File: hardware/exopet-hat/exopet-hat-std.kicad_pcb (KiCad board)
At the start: 2 copper layers, 65 x 56 mm, 77 parts, among them J1 BarrelJack_CUI_PJ-102AH_Horiz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, J10 TerminalBlock_Phoenix_PT-1,5-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, J11 TerminalBlock_Phoenix_PT-1,5-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, J13 TerminalBlock_Phoenix_PT-1,5-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, J14 TerminalBlock_Phoenix_PT-1,5-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, J3 PinSocket_2x20_P2.54mm_Vertic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, J4 TerminalBlock_Phoenix_PT-1,5-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, J8 TerminalBlock_Phoenix_PT-1,5-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, J9 TerminalBlock_Phoenix_PT-1,5-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, K1 Relay_SPDT_Omron-G5LE-1, K2 Relay_SPDT_Omron-G5LE-1, K3 Relay_SPDT_Omron-G5LE-1, K4 Relay_SPDT_Omron-G5LE-1, Q1 TO-252-2, U2 SOIC-16_3.9x9.9mm_P1.27mm, U4 SOIC-8_3.9x4.9mm_P1.27mm, U5 D_SOD-323, U6 SOT-23-6, U7 MSOP-10_3x3mm_P0.5mm

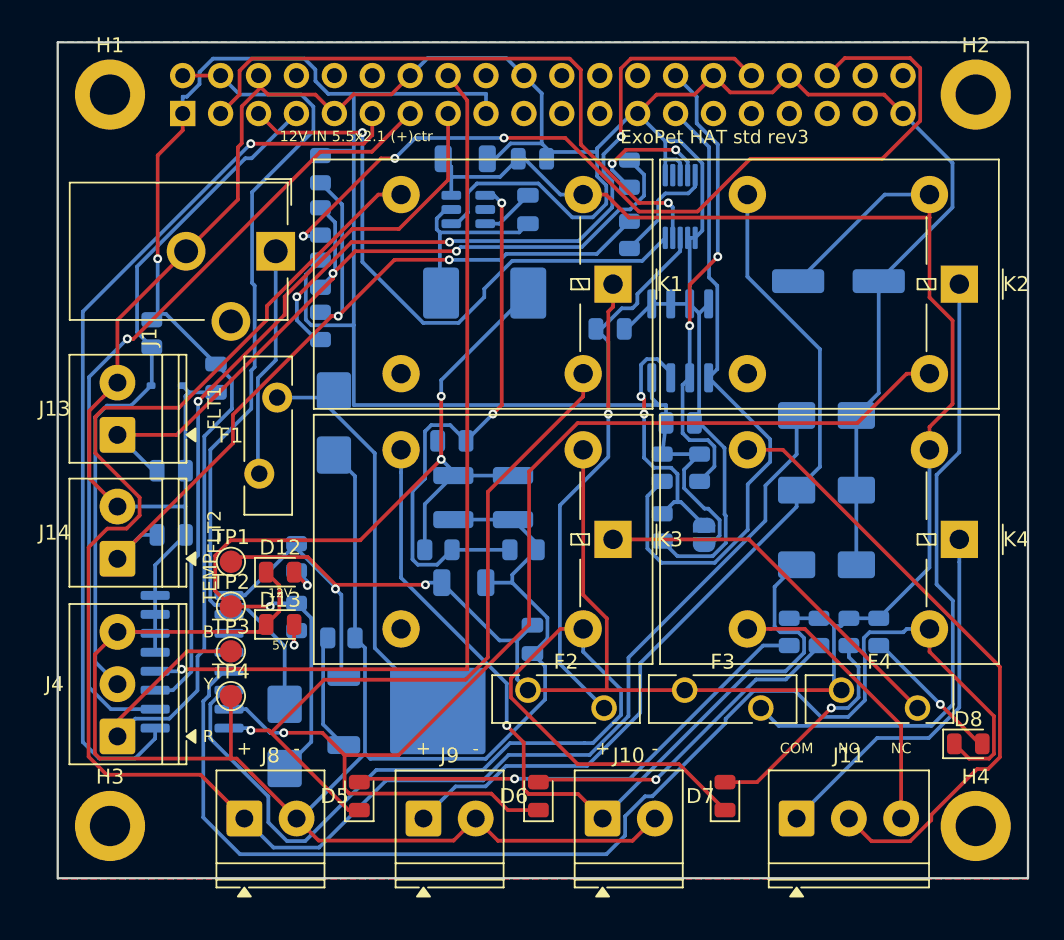
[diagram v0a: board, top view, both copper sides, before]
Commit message: HAT std: verified JLC part numbers + DFM hole-fit pass (13 blanks -> 3)
Researched & datasheet-verified LCSC codes filled for 9 lines (10uF
C14860, 22uF C309062, 100uF elec C3338, 12.7k C17434, 75pF C113832,
ADS1115 C37593, EEPROM 24LC32A C511262, SMBJ16CA C71870, TPS54302
C311983). Each confirmed against a fetched LCSC/JLC page for
value+package match.

DFM FIX (found by this pass): D3 was 'B550C' on a D_SMB footprint, but
B550C is SMC (DO-214AB) — it would NOT fit the SMB holes. Swapped to
SS56(LOWVF) C2891311, a genuine SMB (DO-214AA) 5A 60V schottky and a
JLC *Basic* part. std re-verified fully green.

Through-hole hole-fit check (all PASS): F1 MF-RG700 leads 0.81mm <
1.01mm hole; F2-F4 = C208481 (Bourns MF-R110, 0.51mm leads) < 0.71mm
hole; relays C1524650 match Omron's 1.3mm spec. The rev-1 fuse-leg
rejection cannot recur.

3 lines remain blank by necessity: J1 barrel jack (not in JLC assembly
lib), L1 inductor + F1 7A fuse (no fetch-confirmed LCSC code found —
NOT guessed; hints kept). F1 also needs a decision: MF-RG700 isn't
JLC-stocked and its body is taller than the RG500 footprint.

Co-Authored-By: Claude Fable 5 <noreply@anthropic.com>
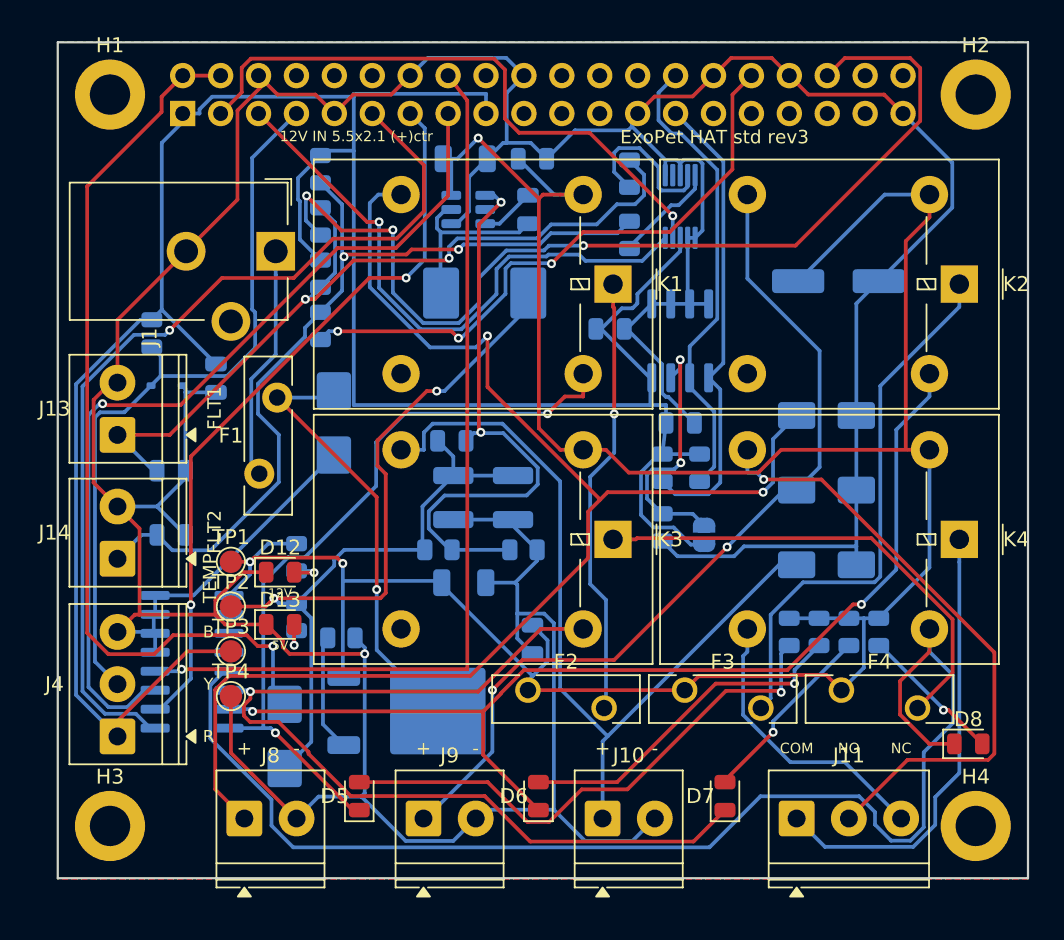
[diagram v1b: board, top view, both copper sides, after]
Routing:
- net CH1_OUT: track 120.5 -> 91.4 mm, vias 0 -> 2
- net GND: track 352.2 -> 330.4 mm, vias 0 -> 1
- net EEPROM_SDA: track 44.6 -> 31.3 mm
- net GPIO22: track 49.3 -> 59.5 mm
- net RLY2_DRV: track 80.6 -> 70.9 mm, vias 1 -> 2
- net +12V: track 171.0 -> 180.3 mm, vias 2 -> 3
- net +5V_BUCK: track 64.4 -> 72.7 mm, vias 3 -> 2
- net CH3_FUSED: track 25.1 -> 32.0 mm
- net FLOAT1_GPIO: track 60.3 -> 67.2 mm
- net RLY3_DRV: track 70.6 -> 64.0 mm, vias 0 -> 1
- net CH2_FUSED: track 43.2 -> 36.7 mm
- net FLOAT2_GPIO: track 46.8 -> 40.5 mm
- net CH4_COM: track 25.2 -> 30.5 mm
- net GPIO27: track 54.6 -> 49.4 mm, vias 1 -> 2
- net +5V: track 55.8 -> 60.6 mm, vias 0 -> 1
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
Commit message: HAT: larger 5.08mm relay terminals on pro; std constrained to 3.5mm
Per request for bigger-wire terminals: relay outputs -> KF301-5.0
(5.08mm pitch, up to 2.5mm2 / 14 AWG, 1.6mm holes vs ~1.1mm pins =
verified fit), matched to the G5LE 10A contact rating. Verified LCSC
codes C474881 (2P) / C474882 (3P), Cixi Kefa, JLC-stocked.

CONSTRAINT FOUND (measured): four 5.08mm terminals need 52.3mm edge-to-
edge but only 49.6mm is free on std's 65mm front edge (between the temp
terminal and the H4 mounting hole) -- they physically do not fit, and
even AUX-only cascades into unsolvable channel-LED crowding on the full
65x56 board. So terminal sizing is variant-conditional: pro (65x92,
roomy) gets 5.08mm on ALL relay channels; std stays 3.5mm (reverted to
green). Footprints (CH_2P/CH_3P) and LCSC codes both keyed by variant;
std re-verified fully green (placement/DRC/golden/fab).

std decision still open: keep 3.5mm, or force AUX-5.08 by moving std's
channel LEDs off the front face.

Co-Authored-By: Claude Fable 5 <noreply@anthropic.com>
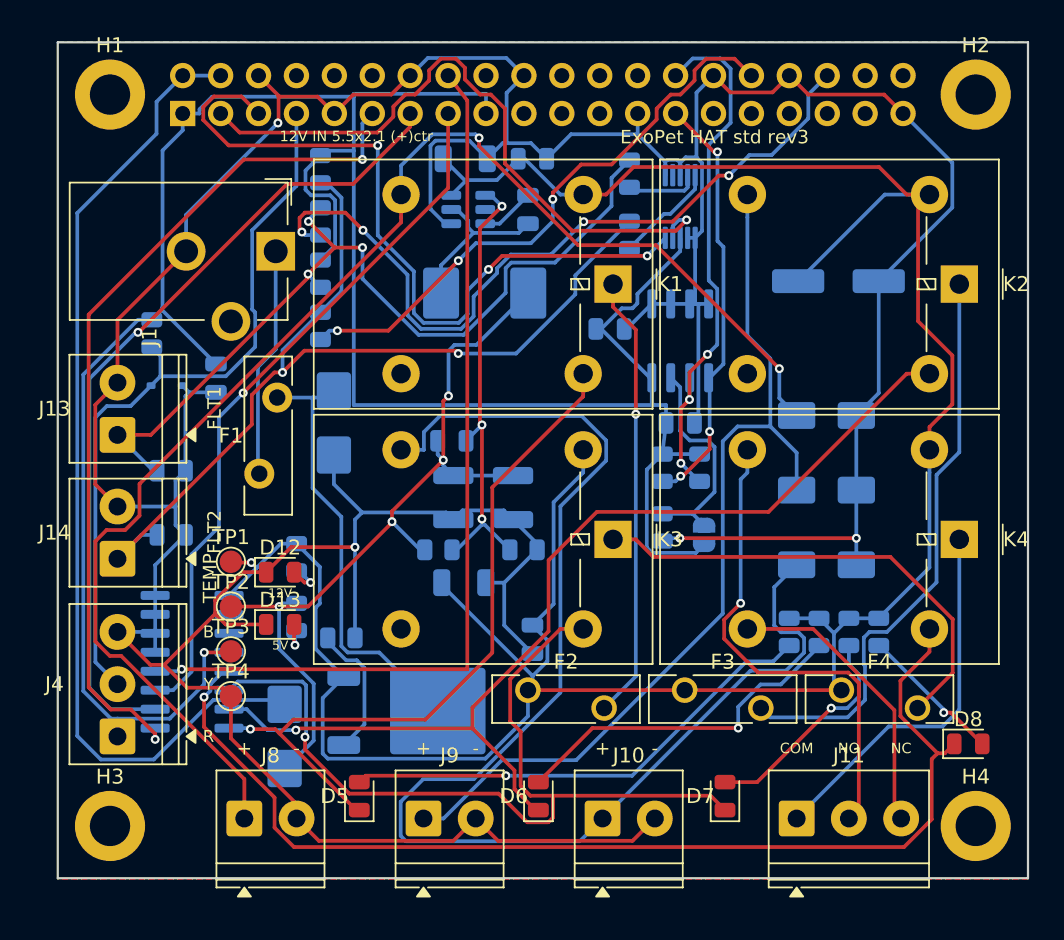
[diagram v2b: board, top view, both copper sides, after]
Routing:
- net CH3_OUT: track 55.1 -> 90.7 mm
- net GND: track 330.4 -> 312.7 mm, vias 1 -> 4
- net +5V_BUCK: track 72.7 -> 56.7 mm, vias 2 -> 4
- net FLOAT1_GPIO: track 67.2 -> 51.6 mm, vias 3 -> 4
- net GPIO22: track 59.5 -> 47.5 mm
- net RLY4_DRV: track 86.3 -> 74.8 mm, vias 0 -> 1
- net I2C1_SCL: track 39.7 -> 50.4 mm, vias 1 -> 3
- net BUCK_FB: track 39.7 -> 30.2 mm, vias 2 -> 3
- net CH4_NO: track 41.4 -> 32.9 mm
- net FLOAT2_SW: track 57.6 -> 64.2 mm
- net RLY3_DRV: track 64.0 -> 58.2 mm
- net FLT1_SENSE: track 10.6 -> 4.91 mm
- net GPIO27: track 49.4 -> 55.0 mm, vias 2 -> 1
- net +5V: track 60.6 -> 66.0 mm, vias 1 -> 0
- net CH4_COM: track 30.5 -> 25.3 mm
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
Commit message: HAT std: AUX dry-contact gets the big 5.08mm terminal (14 AWG)
std's AUX (CH4, J11) -> KF301-5.0 (5.08mm, up to 14 AWG, C474882),
matched to the 10A relay contact. Switched channels CH1-3 stay 3.5mm
(fused 1A). To fit the wider AUX on the packed 65x56 front edge, the
four channel-state LEDs move to the back (rev-1 style) -- a deliberate
trade the user accepted (terminal prioritized over front LED
visibility). flip_backs is now variant-aware (std backs the LEDs; pro
keeps them top). Dry-contact codes variant-independent; switched-
channel codes variant-keyed. std fully green.

Co-Authored-By: Claude Fable 5 <noreply@anthropic.com>
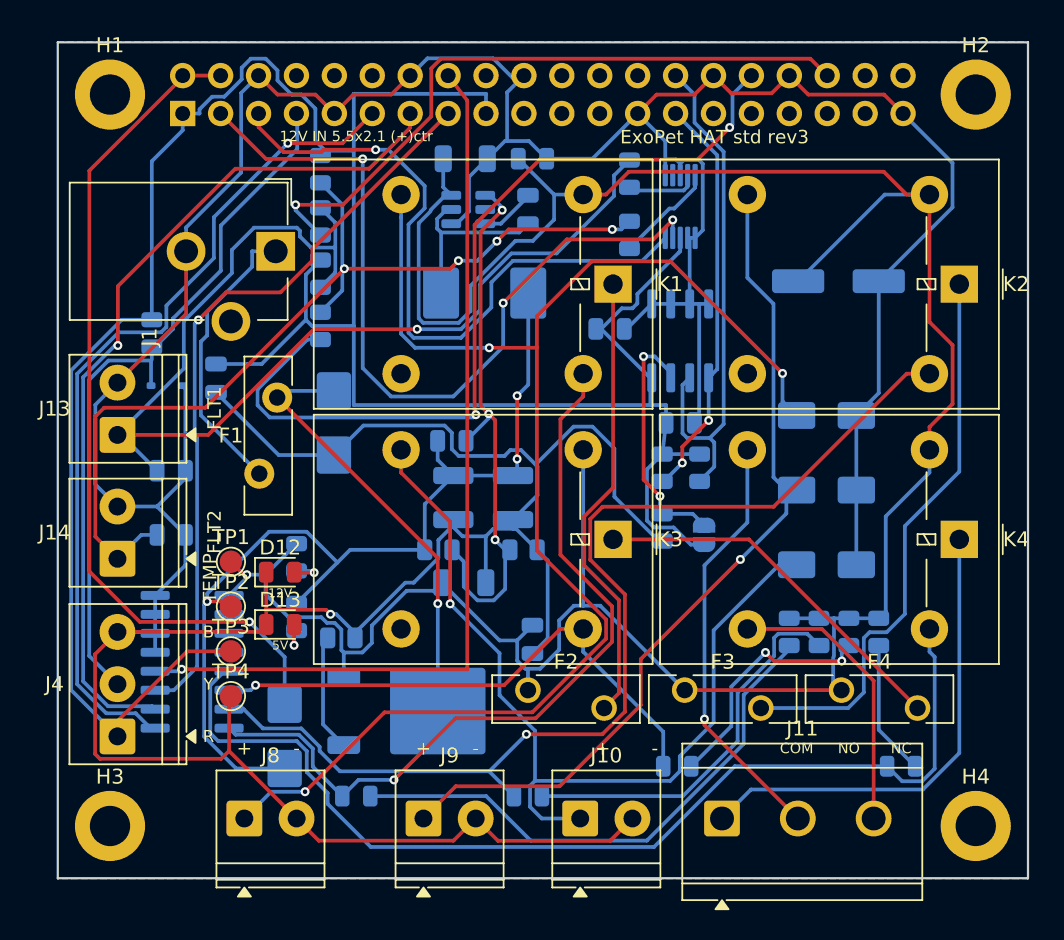
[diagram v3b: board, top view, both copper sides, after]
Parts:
- D5, D6, D7, D8: moved to B.Cu
- J11: value TerminalBlock_Phoenix_PT-1,5-3-3.5-H_1x03_P3.50mm_Horizontal -> TerminalBlock_CUI_TB007-508-03_1x03_P5.08mm_Horizontal; footprint TerminalBlock_Phoenix:TerminalBlock_Phoenix_PT-1,5-3-3.5-H_1x03_P3.50mm_Horizontal -> TerminalBlock_CUI:TerminalBlock_CUI_TB007-508-03_1x03_P5.08mm_Horizontal
- moved J11 5.00 mm to (44.5, 52.0)
- moved D8 4.74 mm to (56.5, 48.5)
- moved D7 3.77 mm to (41.5, 48.5), turned to 0 degrees
- moved J10 1.50 mm to (35.0, 52.0)
- moved D6 0.70 mm to (31.5, 50.5), turned to 0 degrees
- moved D5 0.20 mm to (20.0, 50.5), turned to 0 degrees
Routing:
- net CH3_OUT: track 90.7 -> 59.2 mm, vias 0 -> 1
- net GND: track 312.7 -> 338.6 mm, vias 4 -> 1
- net RLY3_DRV: track 58.2 -> 36.8 mm
- net FLOAT2_GPIO: track 39.1 -> 58.3 mm, vias 3 -> 2
- net FLOAT1_SW: track 58.7 -> 77.3 mm, vias 3 -> 1
- net I2C1_SDA: track 44.2 -> 54.2 mm, vias 1 -> 3
- net +5V: track 66.0 -> 57.0 mm, vias 0 -> 1
- net +5V_BUCK: track 56.7 -> 64.2 mm, vias 4 -> 3
- net BUCK_FB: track 30.2 -> 37.3 mm
- net FLOAT1_GPIO: track 51.6 -> 44.7 mm, vias 4 -> 1
- net CH3_FUSED: track 31.9 -> 25.1 mm
- net CH4_COM: track 25.3 -> 32.0 mm
- net +12V: track 180.0 -> 185.5 mm
- net I2C1_SCL: track 50.4 -> 45.2 mm, vias 3 -> 1
- net RLY2_DRV: track 68.4 -> 73.0 mm
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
